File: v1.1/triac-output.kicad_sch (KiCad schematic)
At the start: 7 parts, among them Q7 BT138-600, Q8 2N7002, U8 TLP160G

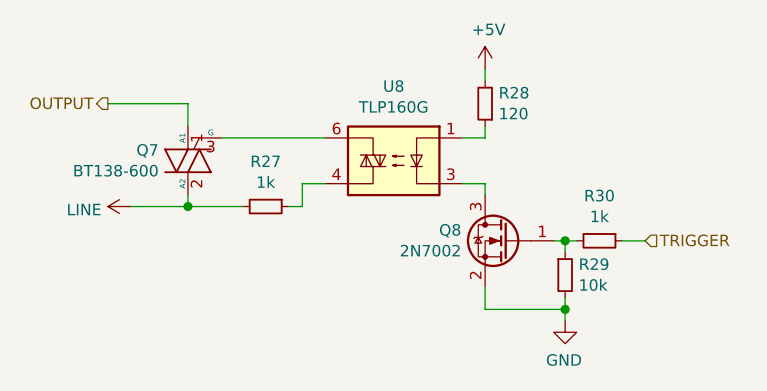
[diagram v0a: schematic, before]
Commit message: start rework to smd triac
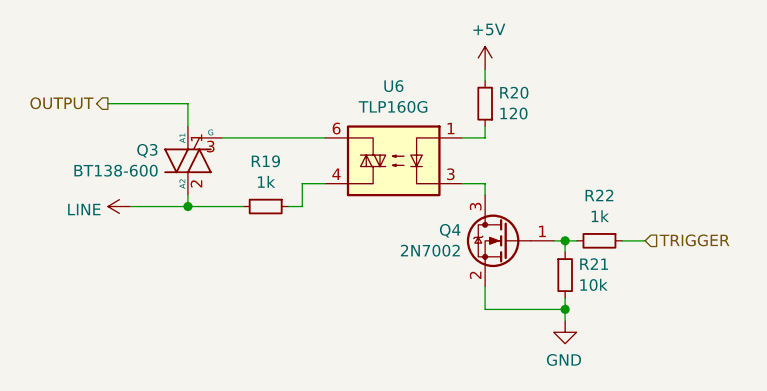
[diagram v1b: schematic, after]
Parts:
- Q3: renamed from Q7; footprint Package_TO_SOT_THT:TO-220-3_Vertical -> Package_TO_SOT_SMD:TO-252-2
- renumbered Q8 to Q4, R27 to R19, R28 to R20, R29 to R21, R30 to R22, U8 to U6
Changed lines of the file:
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@@
   (symbol (lib_id "power:LINE") (at 85.09 57.15 90) (mirror x)
     (in_bom yes) (on_board yes)
-    (property "Reference" "#PWR048" (id 0) (at 88.9 57.15 0)
+    (property "Reference" "#PWR042" (id 0) (at 88.9 57.15 0)
       (effects (font (size 1.27 1.27)) hide)
     )
@@
   (symbol (lib_id "power:+5V") (at 124.46 41.91 0)
     (in_bom yes) (on_board yes)
-    (property "Reference" "#PWR049" (id 0) (at 124.46 45.72 0)
+    (property "Reference" "#PWR043" (id 0) (at 124.46 45.72 0)
       (effects (font (size 1.27 1.27)) hide)
     )
@@
   (symbol (lib_id "power:GND") (at 133.35 69.85 0) (mirror y)
     (in_bom yes) (on_board yes)
-    (property "Reference" "#PWR050" (id 0) (at 133.35 76.2 0)
+    (property "Reference" "#PWR044" (id 0) (at 133.35 76.2 0)
       (effects (font (size 1.27 1.27)) hide)
     )
@@
   (symbol (lib_id "Device:R_Small") (at 100.076 57.15 270)
     (in_bom yes) (on_board yes)
-    (property "Reference" "R27" (id 0) (at 100.076 52.1716 90))
+    (property "Reference" "R19" (id 0) (at 100.076 52.1716 90))
     (property "Value" "1k" (id 1) (at 100.076 54.483 90))
     (property "Footprint" "Resistor_SMD:R_1206_3216Metric_Pad1.30x1.75mm_HandSolder" (id 2) (at 100.076 57.15 0)
@@
   (symbol (lib_id "Device:R_Small") (at 124.46 45.72 180)
     (in_bom yes) (on_board yes)
-    (property "Reference" "R28" (id 0) (at 125.9586 44.5516 0)
+    (property "Reference" "R20" (id 0) (at 125.9586 44.5516 0)
       (effects (font (size 1.27 1.27)) (justify right))
     )
@@
   (symbol (lib_id "Device:R_Small") (at 133.35 64.77 0)
     (in_bom yes) (on_board yes)
-    (property "Reference" "R29" (id 0) (at 134.8486 63.6016 0)
+    (property "Reference" "R21" (id 0) (at 134.8486 63.6016 0)
       (effects (font (size 1.27 1.27)) (justify left))
     )
@@
   (symbol (lib_id "Device:R_Small") (at 137.16 60.96 270)
     (in_bom yes) (on_board yes)
-    (property "Reference" "R30" (id 0) (at 137.16 55.9816 90))
+    (property "Reference" "R22" (id 0) (at 137.16 55.9816 90))
     (property "Value" "1k" (id 1) (at 137.16 58.293 90))
     (property "Footprint" "Resistor_SMD:R_0603_1608Metric_Pad0.98x0.95mm_HandSolder" (id 2) (at 137.16 60.96 0)
@@
   (symbol (lib_id "Triac_Thyristor:BT138-600") (at 91.44 52.07 180)
     (in_bom yes) (on_board yes)
-    (property "Reference" "Q7" (id 0) (at 88.1888 50.9016 0)
+    (property "Reference" "Q3" (id 0) (at 88.1888 50.9016 0)
       (effects (font (size 1.27 1.27)) (justify left))
     )
@@
       (effects (font (size 1.27 1.27)) (justify left))
     )
-    (property "Footprint" "Package_TO_SOT_THT:TO-220-3_Vertical" (id 2) (at 86.36 50.165 0)
+    (property "Footprint" "Package_TO_SOT_SMD:TO-252-2" (id 2) (at 86.36 50.165 0)
       (effects (font (size 1.27 1.27) italic) (justify left) hide)
     )
@@
   (symbol (lib_id "Transistor_FET:2N7002") (at 127 60.96 0) (mirror y)
     (in_bom yes) (on_board yes)
-    (property "Reference" "Q8" (id 0) (at 121.8184 59.7916 0)
+    (property "Reference" "Q4" (id 0) (at 121.8184 59.7916 0)
       (effects (font (size 1.27 1.27)) (justify left))
     )
@@
   (symbol (lib_id "Relay_SolidState:TLP160G") (at 114.3 52.07 0) (mirror y)
     (in_bom yes) (on_board yes)
-    (property "Reference" "U8" (id 0) (at 114.3 43.815 0))
+    (property "Reference" "U6" (id 0) (at 114.3 43.815 0))
     (property "Value" "TLP160G" (id 1) (at 114.3 46.1264 0))
     (property "Footprint" "Package_SO:MFSOP6-4_4.4x3.6mm_P1.27mm" (id 2) (at 114.3 59.69 0)

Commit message: more work on smd triac routing
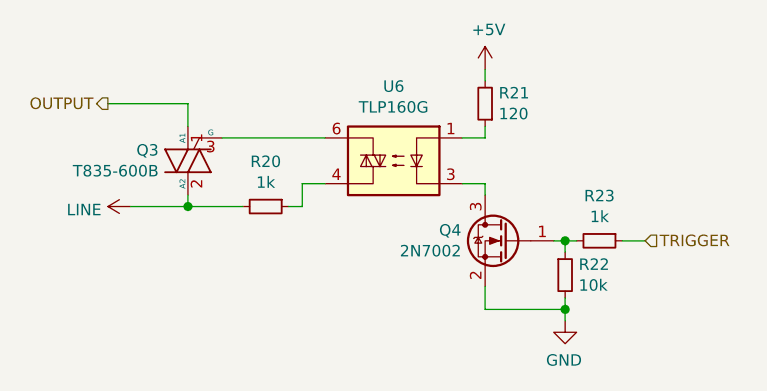
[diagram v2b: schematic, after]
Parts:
- Q3: value BT138-600 -> T835-600B
- renumbered R19 to R20, R20 to R21, R21 to R22, R22 to R23
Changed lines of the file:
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@@
   (symbol (lib_id "power:LINE") (at 85.09 57.15 90) (mirror x)
     (in_bom yes) (on_board yes)
-    (property "Reference" "#PWR042" (id 0) (at 88.9 57.15 0)
+    (property "Reference" "#PWR045" (id 0) (at 88.9 57.15 0)
       (effects (font (size 1.27 1.27)) hide)
     )
@@
   (symbol (lib_id "power:+5V") (at 124.46 41.91 0)
     (in_bom yes) (on_board yes)
-    (property "Reference" "#PWR043" (id 0) (at 124.46 45.72 0)
+    (property "Reference" "#PWR046" (id 0) (at 124.46 45.72 0)
       (effects (font (size 1.27 1.27)) hide)
     )
@@
   (symbol (lib_id "power:GND") (at 133.35 69.85 0) (mirror y)
     (in_bom yes) (on_board yes)
-    (property "Reference" "#PWR044" (id 0) (at 133.35 76.2 0)
+    (property "Reference" "#PWR047" (id 0) (at 133.35 76.2 0)
       (effects (font (size 1.27 1.27)) hide)
     )
@@
   (symbol (lib_id "Device:R_Small") (at 100.076 57.15 270)
     (in_bom yes) (on_board yes)
-    (property "Reference" "R19" (id 0) (at 100.076 52.1716 90))
+    (property "Reference" "R20" (id 0) (at 100.076 52.1716 90))
     (property "Value" "1k" (id 1) (at 100.076 54.483 90))
     (property "Footprint" "Resistor_SMD:R_1206_3216Metric_Pad1.30x1.75mm_HandSolder" (id 2) (at 100.076 57.15 0)
@@
   (symbol (lib_id "Device:R_Small") (at 124.46 45.72 180)
     (in_bom yes) (on_board yes)
-    (property "Reference" "R20" (id 0) (at 125.9586 44.5516 0)
+    (property "Reference" "R21" (id 0) (at 125.9586 44.5516 0)
       (effects (font (size 1.27 1.27)) (justify right))
     )
@@
   (symbol (lib_id "Device:R_Small") (at 133.35 64.77 0)
     (in_bom yes) (on_board yes)
-    (property "Reference" "R21" (id 0) (at 134.8486 63.6016 0)
+    (property "Reference" "R22" (id 0) (at 134.8486 63.6016 0)
       (effects (font (size 1.27 1.27)) (justify left))
     )
@@
   (symbol (lib_id "Device:R_Small") (at 137.16 60.96 270)
     (in_bom yes) (on_board yes)
-    (property "Reference" "R22" (id 0) (at 137.16 55.9816 90))
+    (property "Reference" "R23" (id 0) (at 137.16 55.9816 90))
     (property "Value" "1k" (id 1) (at 137.16 58.293 90))
     (property "Footprint" "Resistor_SMD:R_0603_1608Metric_Pad0.98x0.95mm_HandSolder" (id 2) (at 137.16 60.96 0)
@@
       (effects (font (size 1.27 1.27)) (justify left))
     )
-    (property "Value" "BT138-600" (id 1) (at 88.1888 53.213 0)
+    (property "Value" "T835-600B" (id 1) (at 88.1888 53.213 0)
       (effects (font (size 1.27 1.27)) (justify left))
     )

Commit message: more routing
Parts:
- R20: value 1k -> 360R/0.5W; Part (none) -> Panasonic ERJP08F3600V
- R21: value 120 -> 360R
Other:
- title: (none) -> MadPresso controller
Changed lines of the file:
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@@
   (page 0 6)
   (paper "A5")
+  (title_block
+    (title "MadPresso controller")
+    (date "2020-11-18")
+    (rev "1.1")
+  )
   (junction (at 91.44 57.15) (diameter 1.016) (color 0 0 0 0))
   (junction (at 133.35 60.96) (diameter 1.016) (color 0 0 0 0))
@@
   (symbol (lib_id "power:LINE") (at 85.09 57.15 90) (mirror x)
     (in_bom yes) (on_board yes)
-    (property "Reference" "#PWR051" (id 0) (at 88.9 57.15 0)
+    (property "Reference" "#PWR045" (id 0) (at 88.9 57.15 0)
       (effects (font (size 1.27 1.27)) hide)
     )
@@
   (symbol (lib_id "power:+5V") (at 124.46 41.91 0)
     (in_bom yes) (on_board yes)
-    (property "Reference" "#PWR052" (id 0) (at 124.46 45.72 0)
+    (property "Reference" "#PWR046" (id 0) (at 124.46 45.72 0)
       (effects (font (size 1.27 1.27)) hide)
     )
@@
   (symbol (lib_id "power:GND") (at 133.35 69.85 0) (mirror y)
     (in_bom yes) (on_board yes)
-    (property "Reference" "#PWR053" (id 0) (at 133.35 76.2 0)
+    (property "Reference" "#PWR047" (id 0) (at 133.35 76.2 0)
       (effects (font (size 1.27 1.27)) hide)
     )
@@
   (symbol (lib_id "Device:R_Small") (at 100.076 57.15 270)
     (in_bom yes) (on_board yes)
-    (property "Reference" "R20" (id 0) (at 100.076 52.1716 90))
-    (property "Value" "1k" (id 1) (at 100.076 54.483 90))
+    (property "Reference" "R20" (id 0) (at 100.076 54.7116 90))
+    (property "Value" "360R/0.5W" (id 1) (at 100.076 59.563 90))
     (property "Footprint" "Resistor_SMD:R_1206_3216Metric_Pad1.30x1.75mm_HandSolder" (id 2) (at 100.076 57.15 0)
       (effects (font (size 1.27 1.27)) hide)
     )
-    (property "Datasheet" "~" (id 3) (at 100.076 57.15 0)
+    (property "Datasheet" "https://docs.rs-online.com/ef78/0900766b812cb812.pdf" (id 3) (at 100.076 57.15 0)
+      (effects (font (size 1.27 1.27)) hide)
+    )
+    (property "Part" "Panasonic ERJP08F3600V" (id 4) (at 100.076 57.15 90)
       (effects (font (size 1.27 1.27)) hide)
     )
@@
       (effects (font (size 1.27 1.27)) (justify right))
     )
-    (property "Value" "120" (id 1) (at 125.9586 46.863 0)
+    (property "Value" "360R" (id 1) (at 125.9586 46.863 0)
       (effects (font (size 1.27 1.27)) (justify right))
     )

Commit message: some more documentation
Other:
- note added: "Ensure a voltage safety of at least 357 Veff ((230 VAC * sqrt(2))+ 10%) for the triac gate resistor!"
- moved on the sheet: Q3, R20

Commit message: v1.1a
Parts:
- renumbered Q3 to Q7, Q4 to Q8, R20 to R28, R21 to R29, R22 to R30, R23 to R31, U6 to U8
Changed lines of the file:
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@@
   (symbol (lib_id "power:LINE") (at 82.55 57.15 90) (mirror x)
     (in_bom yes) (on_board yes)
-    (property "Reference" "#PWR045" (id 0) (at 86.36 57.15 0)
+    (property "Reference" "#PWR051" (id 0) (at 86.36 57.15 0)
       (effects (font (size 1.27 1.27)) hide)
     )
@@
   (symbol (lib_id "power:+5V") (at 124.46 41.91 0)
     (in_bom yes) (on_board yes)
-    (property "Reference" "#PWR046" (id 0) (at 124.46 45.72 0)
+    (property "Reference" "#PWR052" (id 0) (at 124.46 45.72 0)
       (effects (font (size 1.27 1.27)) hide)
     )
@@
   (symbol (lib_id "power:GND") (at 133.35 69.85 0) (mirror y)
     (in_bom yes) (on_board yes)
-    (property "Reference" "#PWR047" (id 0) (at 133.35 76.2 0)
+    (property "Reference" "#PWR053" (id 0) (at 133.35 76.2 0)
       (effects (font (size 1.27 1.27)) hide)
     )
@@
   (symbol (lib_id "Device:R_Small") (at 97.79 57.15 270)
     (in_bom yes) (on_board yes)
-    (property "Reference" "R20" (id 0) (at 97.79 54.7116 90))
+    (property "Reference" "R28" (id 0) (at 97.79 54.7116 90))
     (property "Value" "360R/0.5W" (id 1) (at 97.79 59.563 90))
     (property "Footprint" "Resistor_SMD:R_1206_3216Metric_Pad1.30x1.75mm_HandSolder" (id 2) (at 97.79 57.15 0)
@@
   (symbol (lib_id "Device:R_Small") (at 124.46 45.72 180)
     (in_bom yes) (on_board yes)
-    (property "Reference" "R21" (id 0) (at 125.9586 44.5516 0)
+    (property "Reference" "R29" (id 0) (at 125.9586 44.5516 0)
       (effects (font (size 1.27 1.27)) (justify right))
     )
@@
   (symbol (lib_id "Device:R_Small") (at 133.35 64.77 0)
     (in_bom yes) (on_board yes)
-    (property "Reference" "R22" (id 0) (at 134.8486 63.6016 0)
+    (property "Reference" "R30" (id 0) (at 134.8486 63.6016 0)
       (effects (font (size 1.27 1.27)) (justify left))
     )
@@
   (symbol (lib_id "Device:R_Small") (at 137.16 60.96 270)
     (in_bom yes) (on_board yes)
-    (property "Reference" "R23" (id 0) (at 137.16 55.9816 90))
+    (property "Reference" "R31" (id 0) (at 137.16 55.9816 90))
     (property "Value" "1k" (id 1) (at 137.16 58.293 90))
     (property "Footprint" "Resistor_SMD:R_0603_1608Metric_Pad0.98x0.95mm_HandSolder" (id 2) (at 137.16 60.96 0)
@@
   (symbol (lib_id "Triac_Thyristor:BT138-600") (at 88.9 52.07 180)
     (in_bom yes) (on_board yes)
-    (property "Reference" "Q3" (id 0) (at 85.6488 50.9016 0)
+    (property "Reference" "Q7" (id 0) (at 85.6488 50.9016 0)
       (effects (font (size 1.27 1.27)) (justify left))
     )
@@
   (symbol (lib_id "Transistor_FET:2N7002") (at 127 60.96 0) (mirror y)
     (in_bom yes) (on_board yes)
-    (property "Reference" "Q4" (id 0) (at 121.8184 59.7916 0)
+    (property "Reference" "Q8" (id 0) (at 121.8184 59.7916 0)
       (effects (font (size 1.27 1.27)) (justify left))
     )
@@
   (symbol (lib_id "Relay_SolidState:TLP160G") (at 114.3 52.07 0) (mirror y)
     (in_bom yes) (on_board yes)
-    (property "Reference" "U6" (id 0) (at 114.3 43.815 0))
+    (property "Reference" "U8" (id 0) (at 114.3 43.815 0))
     (property "Value" "TLP160G" (id 1) (at 114.3 46.1264 0))
     (property "Footprint" "Package_SO:MFSOP6-4_4.4x3.6mm_P1.27mm" (id 2) (at 114.3 59.69 0)
